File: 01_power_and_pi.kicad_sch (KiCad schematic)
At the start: 34 parts, among them J1 XT60 PIGTAIL, J9 PI POWER OUT, U1 LM2596S-5.0, U4 TPS54560BDDA

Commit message: Complete pre-PCB electrical and safety audit
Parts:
- removed C38, C39: 220 uF 10 V, Capacitor_THT:CP_Radial_D8.0mm_P3.50mm, symbol Device:C_Polarized
- added C38, C39: 47 uF 10 V X7R, Capacitor_SMD:C_1210_3225Metric, symbol Device:C
- added D14, D2: BAT54, Diode_SMD:D_SOD-323, symbol Device:D_Schottky
- added J18: EXTERNAL LATCHING E-STOP, TerminalBlock:TerminalBlock_MaiXu_MX126-5.0-02P_1x02_P5.00mm, symbol Connector_Generic:Conn_01x02
- added TP1: BAT_RAW, TestPoint:TestPoint_Loop_D2.50mm_Drill1.0mm, symbol Connector:TestPoint
- added TP2: VBAT_SW, TestPoint:TestPoint_Loop_D2.50mm_Drill1.0mm, symbol Connector:TestPoint
- added TP3: ACT_VBAT, TestPoint:TestPoint_Loop_D2.50mm_Drill1.0mm, symbol Connector:TestPoint
- added TP4: +5V_CTRL, TestPoint:TestPoint_Loop_D2.50mm_Drill1.0mm, symbol Connector:TestPoint
- added TP5: PI_5V, TestPoint:TestPoint_Loop_D2.50mm_Drill1.0mm, symbol Connector:TestPoint
- added TP6: GND, TestPoint:TestPoint_Loop_D2.50mm_Drill1.0mm, symbol Connector:TestPoint
- C1: value 1000 uF 25 V -> 1000 uF 35 V
- C30: value 1000 uF 10 V -> 470 uF 10 V LOW ESR
- C36: value 4.7 nF -> 5.1 nF
- C44: value 1 uF 10 V -> 47 uF 10 V X7R; footprint Capacitor_SMD:C_0805_2012Metric -> Capacitor_SMD:C_1210_3225Metric
- D1: value SMBJ18A -> SMBJ15A
- F1: value 15 A EXTERNAL BLADE -> 15 A ATO BLADE
- F3: value 5 A -> 5 A MINI BLADE; footprint Fuse:Fuse_1206_3216Metric -> Fuse:Fuseholder_Blade_Mini_Keystone_3568
- R31: value 442 k -> 54.9 k 1%
- R32: value 90.9 k -> 10.2 k 1%
- R33: value 10.2 k -> 16.9 k 1%
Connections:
- net +5V_CTRL: now also TP4.1
- net BAT_RAW: now also TP1.1
- net GND: now also C38.2, C39.2, D2.1 (K), TP6.1
- net GPIO33_BAT_ADC: now also D14.1 (K), D2.2 (A)
- net PI_5V: now also TP5.1
- net PI_5V_RAW: now also C38.1, C39.1
- net VBAT_SW: now also J18.1 (Pin_1), TP2.1
- new net 3V3: D14.2 (A)
- new net ACT_VBAT: J18.2 (Pin_2), TP3.1
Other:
- note added: "J18 must be closed by a latching E-stop switch. It removes actuator power but keeps Pi/ESP logic alive."
- note removed: "Put the external latching E-stop between F1 and the VBAT_SW distribution point."

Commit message: Correct critical controller schematic safety issues
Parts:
- added C68: DNP SNUBBER 1 nF, Capacitor_SMD:C_0805_2012Metric, symbol Device:C
- added D21: SMBJ15CA ACT TVS, Diode_SMD:D_SMB, symbol Device:D_TVS
- added R34: 267 k 1%, Resistor_SMD:R_0805_2012Metric, symbol Device:R
- added R35: 34.0 k 1%, Resistor_SMD:R_0805_2012Metric, symbol Device:R
- added R36: DNP SNUBBER 10 R, Resistor_SMD:R_0805_2012Metric, symbol Device:R
- C1: footprint Capacitor_THT:CP_Radial_D10.0mm_P5.00mm -> Capacitor_THT:CP_Radial_D12.5mm_P5.00mm
- C30: value 470 uF 10 V LOW ESR -> DNP OPTIONAL BULK 470 uF 10 V; now not fitted
- C32, C33, C34, C35: value 2.2 uF 25 V -> 2.2 uF 25 V X7R
- C7: value 330 uF 10 V -> 330 uF 10 V ESR QUALIFIED
- D1: value SMBJ15A -> SMBJ15CA
- D14: value BAT54 -> BAT54 HIGH CLAMP
- D2: value BAT54 -> BAT54 LOW CLAMP
- J1: value XT60 PIGTAIL -> AMASS XT60PW-M BATTERY INPUT; footprint TerminalBlock:TerminalBlock_MaiXu_MX126-5.0-02P_1x02_P5.00mm -> Connector_AMASS:AMASS_XT60PW-M_1x02_P7.20mm_Horizontal
- J18: value EXTERNAL LATCHING E-STOP -> EXTERNAL DC-RATED LATCHING E-STOP; footprint TerminalBlock:TerminalBlock_MaiXu_MX126-5.0-02P_1x02_P5.00mm -> TerminalBlock_Phoenix:TerminalBlock_Phoenix_MKDS-3-2-5.08_1x02_P5.08mm_Horizontal
- TP1, TP2, TP3, TP4, TP5, TP6: footprint TestPoint:TestPoint_Loop_D2.50mm_Drill1.0mm -> TestPoint:TestPoint_Pad_D1.5mm; now left out of the parts list
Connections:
- net 3V3: now also D14.1 (K); no longer D14.2 (A)
- net ACT_VBAT: now also D21.1 (A1)
- net BAT_RAW: now also J1.2 (Pin_2); no longer J1.1 (Pin_1)
- net CTRL_SW: now also D3.1 (K); no longer D3.2 (A)
- net GND: now also D1.2 (A2), D2.2 (A), D3.2 (A), D9.2 (A), J1.1 (Pin_1), C68.2, D21.2 (A2), R35.2; no longer D1.1 (A1), D2.1 (K), D3.1 (K), D9.1 (K), J1.2 (Pin_2)
- net GPIO33_BAT_ADC: now also D14.2 (A), D2.1 (K); no longer D14.1 (K), D2.2 (A)
- net PI_BUCK_SW: now also D9.1 (K), R36.1; no longer D9.2 (A)
- net VBAT_SW: now also D1.1 (A1), R34.1; no longer D1.2 (A2), U4.3 (EN)
- new net PI_EN_UVLO: R34.2, R35.1, U4.3 (EN)
- new net PI_SNUB: C68.1, R36.2

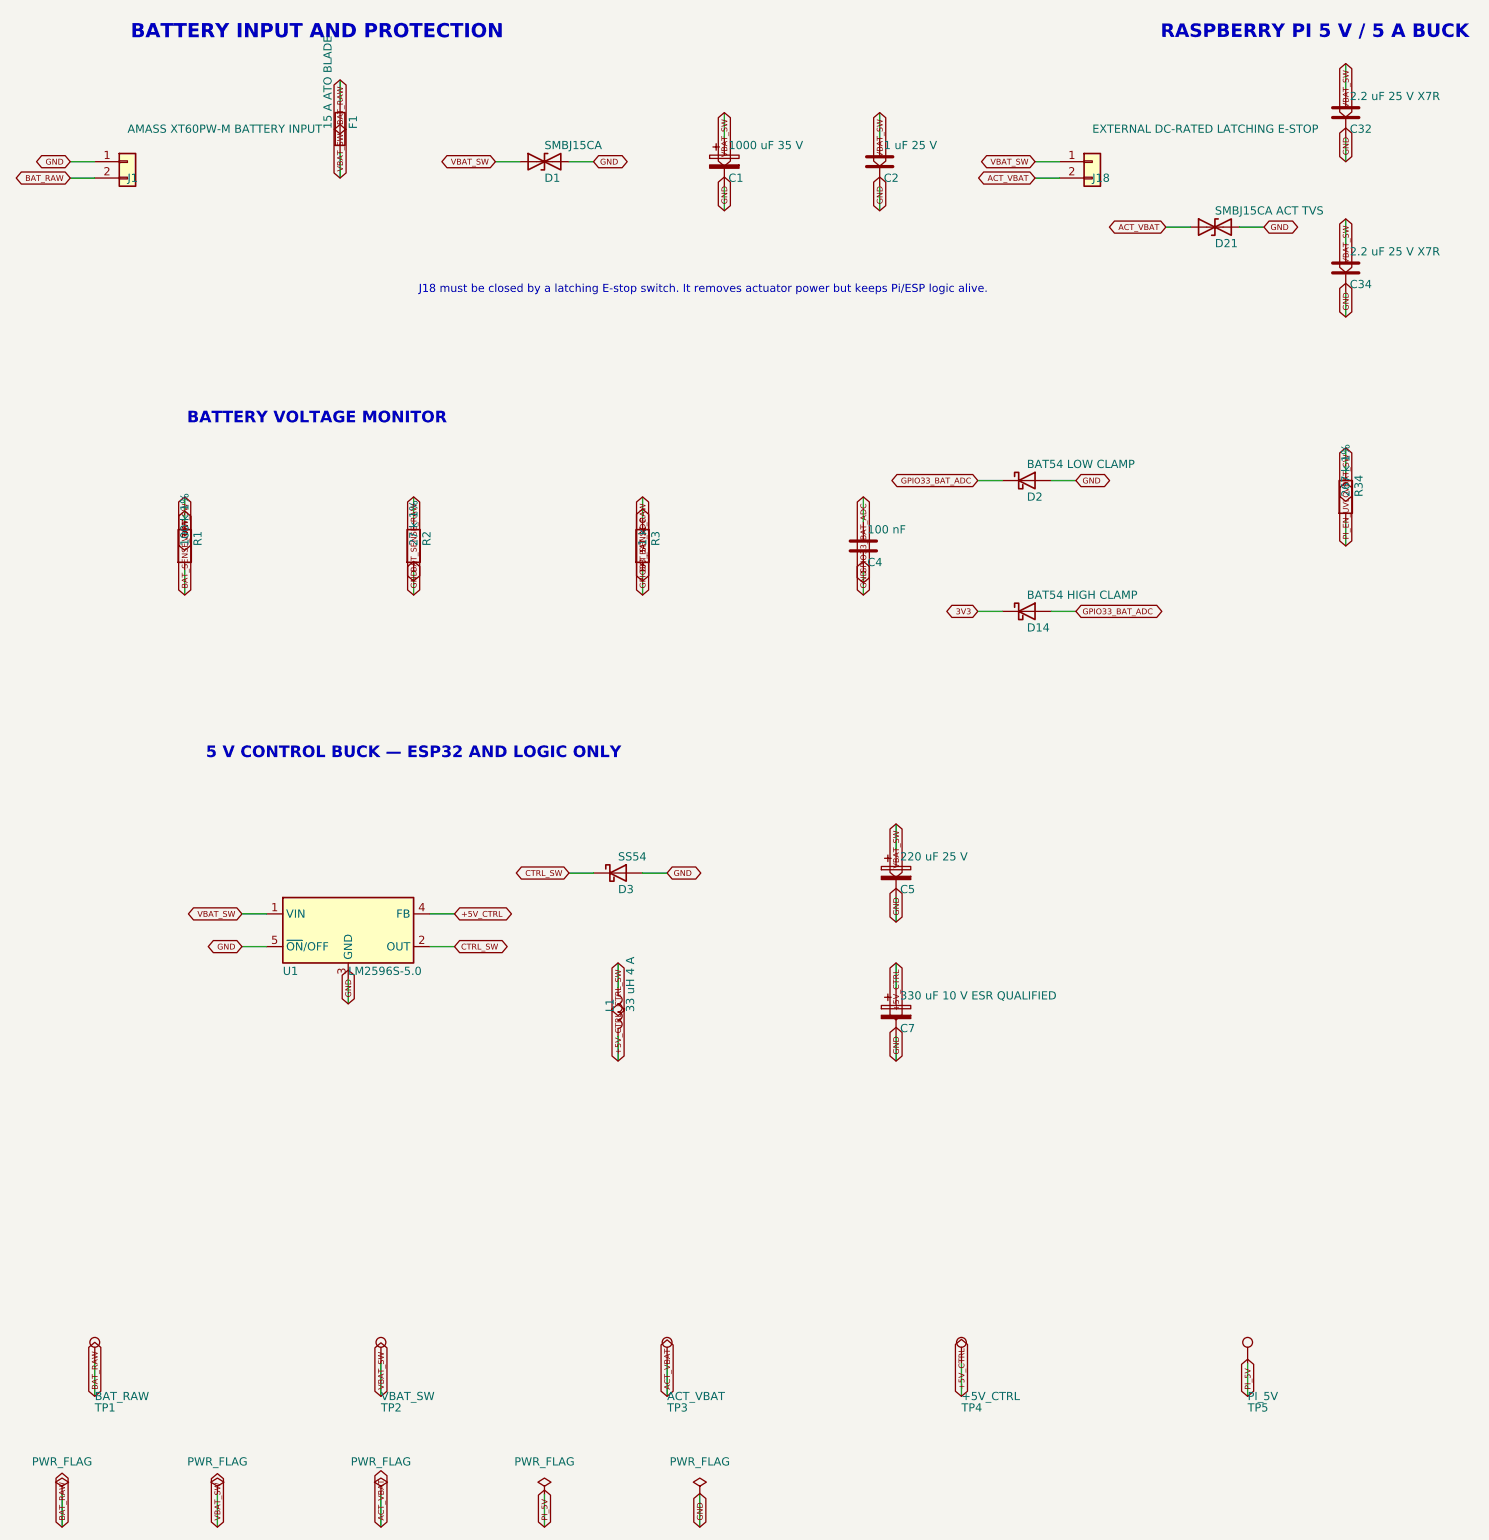
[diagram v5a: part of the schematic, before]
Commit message: Add whole-system battery cutoff and hardened servo interfaces
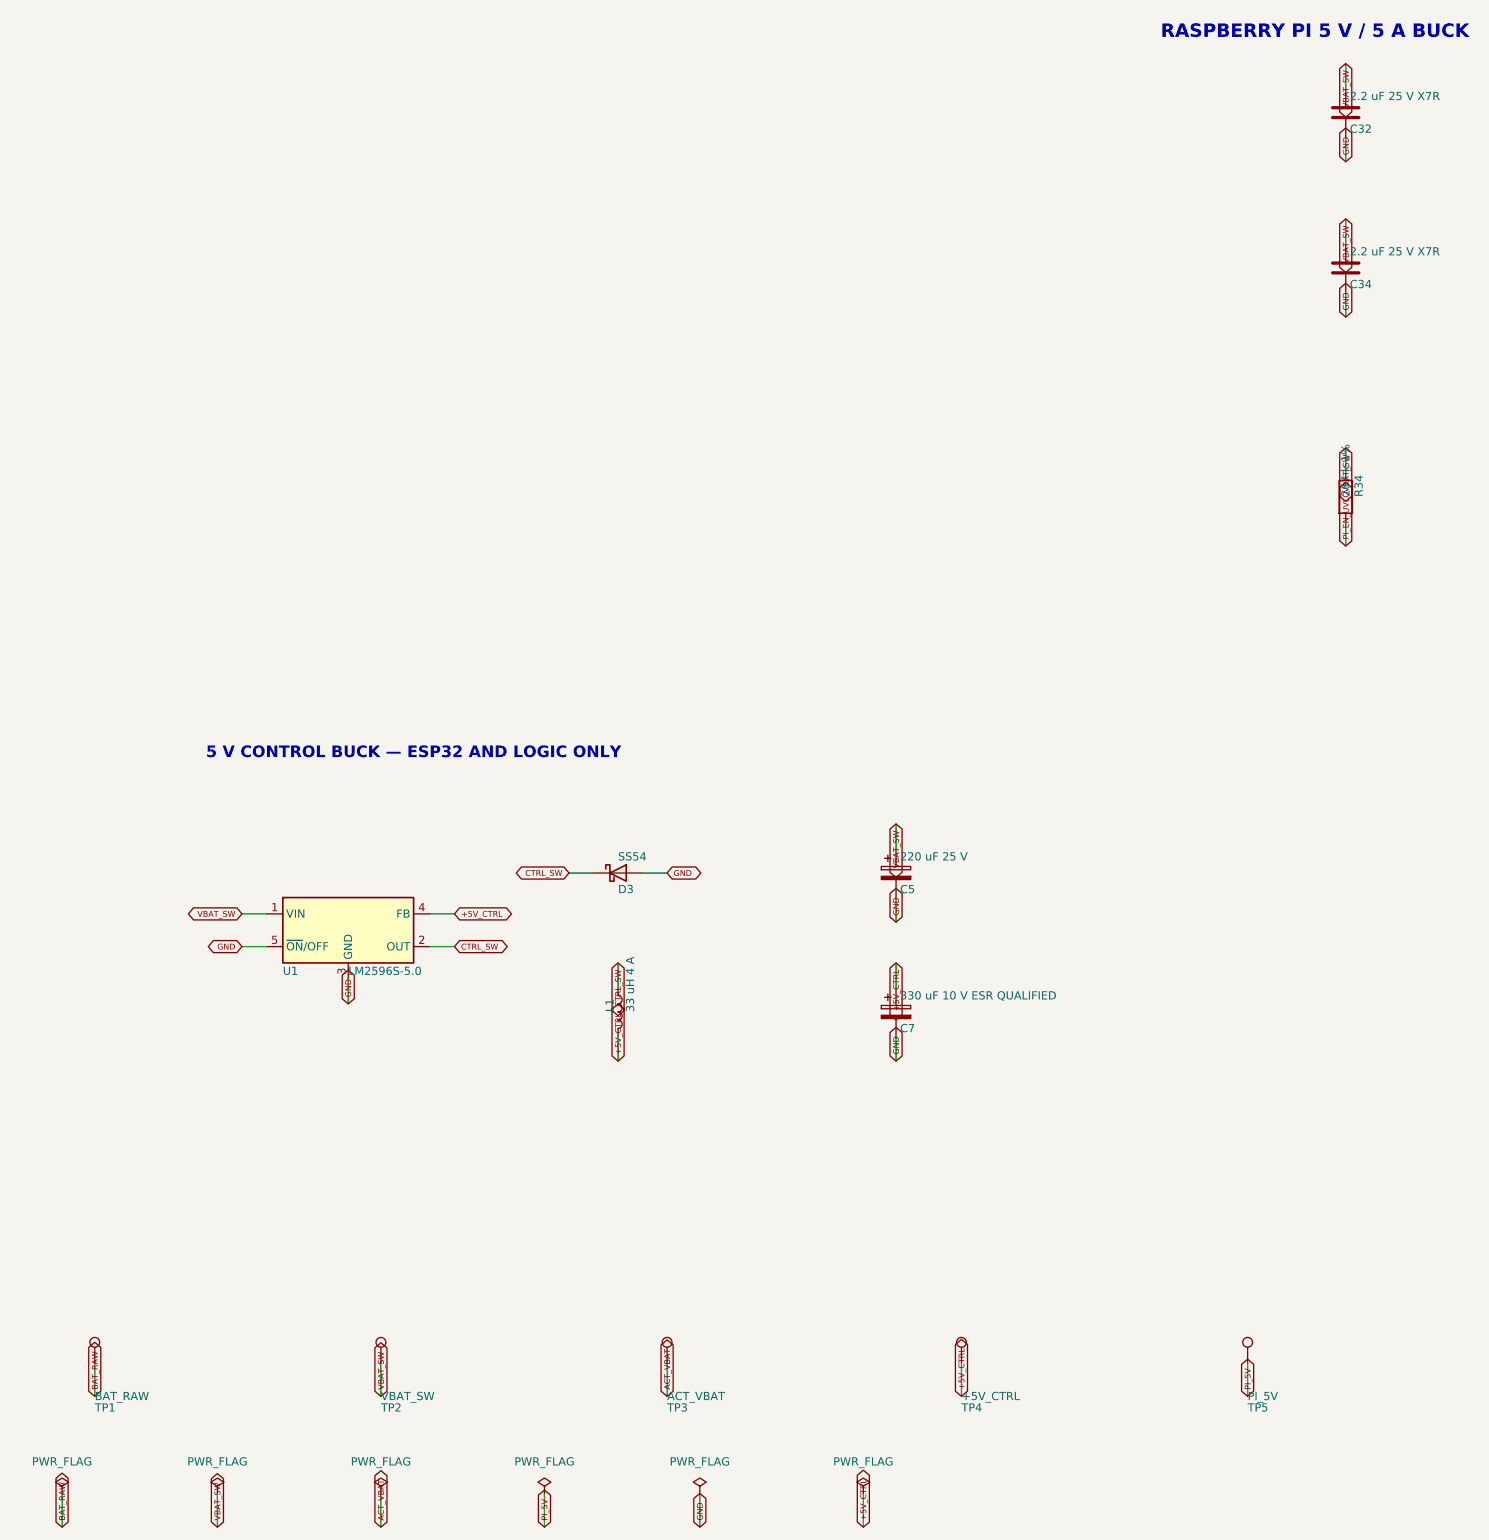
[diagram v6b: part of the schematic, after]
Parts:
- removed C1: 1000 uF 35 V, Capacitor_THT:CP_Radial_D12.5mm_P5.00mm, symbol Device:C_Polarized
- removed C2: 1 uF 25 V, Capacitor_SMD:C_0805_2012Metric, symbol Device:C
- removed C4: 100 nF, Capacitor_SMD:C_0805_2012Metric, symbol Device:C
- removed D1: SMBJ15CA, Diode_SMD:D_SMB, symbol Device:D_TVS
- removed D14: BAT54 HIGH CLAMP, Diode_SMD:D_SOD-323, symbol Device:D_Schottky
- removed D2: BAT54 LOW CLAMP, Diode_SMD:D_SOD-323, symbol Device:D_Schottky
- removed D21: SMBJ15CA ACT TVS, Diode_SMD:D_SMB, symbol Device:D_TVS
- removed F1: 15 A ATO BLADE, Fuse:Fuse_Blade_ATO_directSolder, symbol Device:Fuse
- removed J1: AMASS XT60PW-M BATTERY INPUT, Connector_AMASS:AMASS_XT60PW-M_1x02_P7.20mm_Horizontal, symbol Connector_Generic:Conn_01x02
- removed J18: EXTERNAL DC-RATED LATCHING E-STOP, TerminalBlock_Phoenix:TerminalBlock_Phoenix_MKDS-3-2-5.08_1x02_P5.08mm_Horizontal, symbol Connector_Generic:Conn_01x02
- removed R1: 100 k 1%, Resistor_SMD:R_0805_2012Metric, symbol Device:R
- removed R2: 27 k 1%, Resistor_SMD:R_0805_2012Metric, symbol Device:R
- removed R3: 1 k, Resistor_SMD:R_0805_2012Metric, symbol Device:R
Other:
- note removed: "BATTERY INPUT AND PROTECTION"
- note removed: "BATTERY VOLTAGE MONITOR"
- note removed: "J18 must be closed by a latching E-stop switch. It removes actuator power but keeps Pi/ESP logic alive."
- title: Battery Protection, Logic Buck, and Raspberry Pi Power -> Logic Buck and Raspberry Pi Power
